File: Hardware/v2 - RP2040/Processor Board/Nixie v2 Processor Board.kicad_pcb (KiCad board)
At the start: 2 copper layers, 100 x 50 mm, 75 parts, among them J1 Conn_01x10_Socket, J2 Conn_01x10_Socket, J3 Conn_01x10_Socket, J4 Conn_01x01_Pin, J5 AudioJack3_SwitchT, J6 USB_C_Receptacle_USB2.0, J7 Conn_01x03_2.54mm, J8 Conn_01x03_2.54mm, SW1 SW_Push, SW2 SW_Push, SW3 SW_DIP_x10, SW4 SW_Push, U1 TPS82084SIL, U2 AP22913, U3 DS3231MZ, U4 RP2040, U5 W25Q128JVP, U6 MCP23017_ML, Y1 12MHz

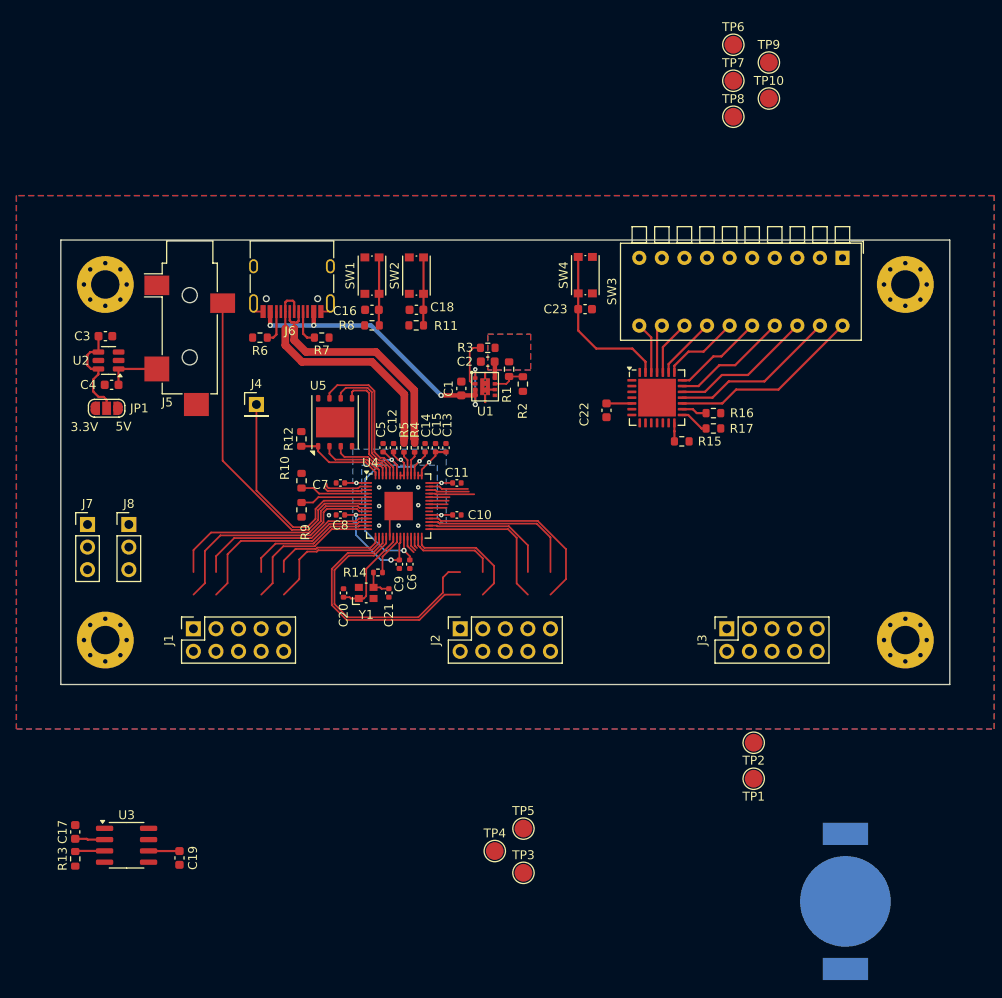
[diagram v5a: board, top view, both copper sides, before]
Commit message: finished initial layout and swapped SDA/SCL on connector
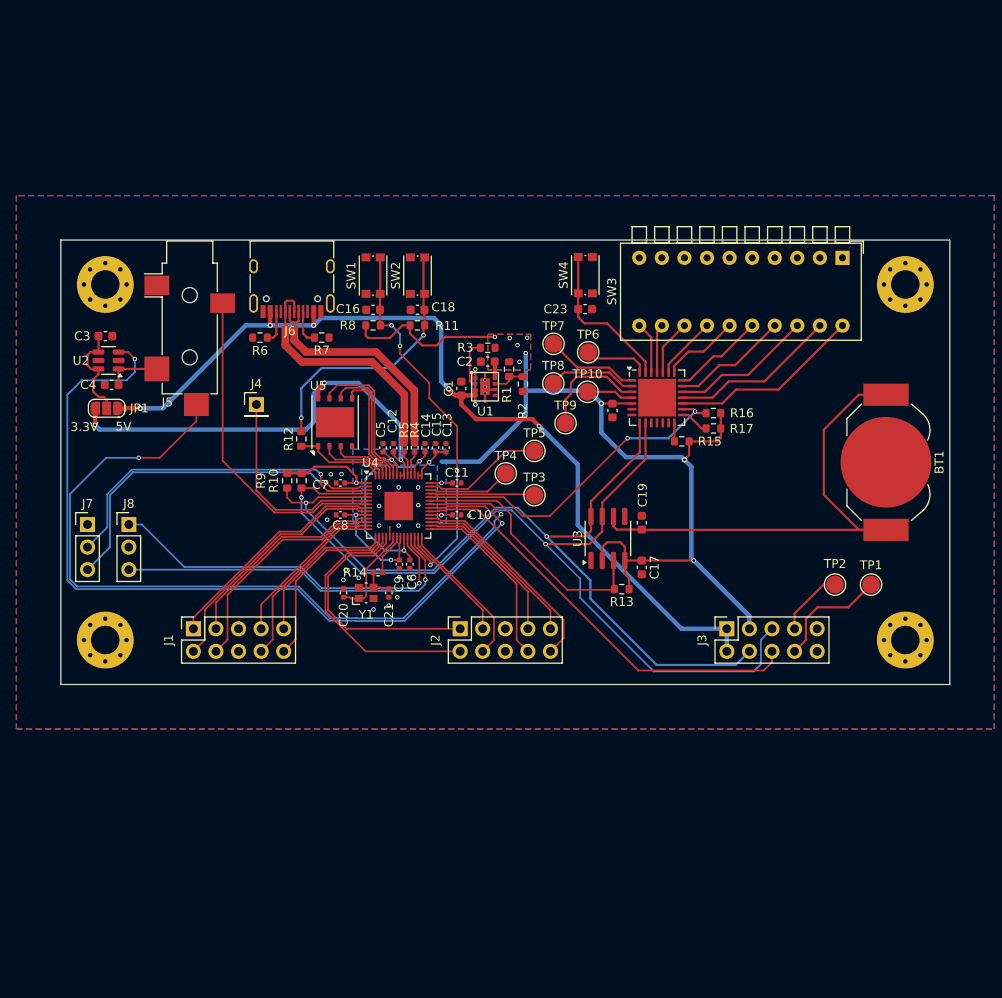
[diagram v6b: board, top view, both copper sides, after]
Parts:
- BT1: moved to F.Cu
- moved C17 70.3 mm to (165.3, 86.8), turned to -90 degrees
- moved R13 68.6 mm to (163.1, 89.3), turned to 180 degrees
- moved C19 64.2 mm to (165.3, 81.8), turned to 90 degrees
- moved U3 64.2 mm to (161.5, 83.6), turned to 90 degrees
- moved BT1 49.6 mm to (192.8, 75.0), turned to 90 degrees
- moved TP9 46.6 mm to (156.8, 70.6)
- moved TP3 42.5 mm to (153.3, 78.7)
- moved TP4 42.5 mm to (150.1, 76.2)
- moved TP5 42.5 mm to (153.3, 73.7)
- moved TP10 38.8 mm to (159.2, 67.1)
- moved TP6 38.3 mm to (159.3, 62.6)
- moved TP8 36.2 mm to (155.4, 66.1)
- moved TP7 35.8 mm to (155.4, 61.7)
- moved TP1 25.5 mm to (191.1, 88.8), turned to -90 degrees
- moved TP2 20.0 mm to (187.1, 88.8), turned to -90 degrees
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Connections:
- net /BOOT_SEL renamed Net-(U4-QSPI_SS)
- J3 pad 4: /I2C1_SDA -> /I2C1_SCL
- J3 pad 5: /I2C1_SCL -> /I2C1_SDA
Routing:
- net +3V3: track 38.1 -> 200.9 mm, vias 7 -> 18
- net /GPS_Enable: track 1.96 -> 97.6 mm, vias 0 -> 2
- net /I2C1_SDA: track 7.75 -> 102.8 mm, vias 0 -> 2
- net /GPS_Connected: track 2.09 -> 93.3 mm, vias 0 -> 2
- net /I2C1_SCL: track 7.74 -> 95.9 mm, vias 0 -> 2
- net VBUS: track 36.0 -> 109.3 mm, vias 5 -> 7
- net Net-(BT1-+): track 3.48 -> 56.6 mm
- net /Dimming: track 0.00 -> 47.8 mm
- net Net-(J8-Pin_1): track 2.05 -> 41.7 mm, vias 0 -> 1
- net Net-(J8-Pin_3): track 1.73 -> 40.7 mm, vias 0 -> 1
- net /UART0 TX: track 5.11 -> 40.3 mm, vias 0 -> 1
- net /RESET: track 9.07 -> 44.1 mm, vias 0 -> 4
- net /UART0 RX: track 5.06 -> 39.0 mm, vias 0 -> 1
- net /Settings_Interrupt: track 5.15 -> 38.5 mm, vias 0 -> 2
- net /RTC_Interrupt: track 5.51 -> 29.5 mm
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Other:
- board text removed: "DCDC"
- board text removed: "GPS"
- board text removed: "INTERCONNECT"
- board text removed: "RP2040"
- board text removed: "RTC"
- board text removed: "SETTINGS"
- board text removed: "USB"

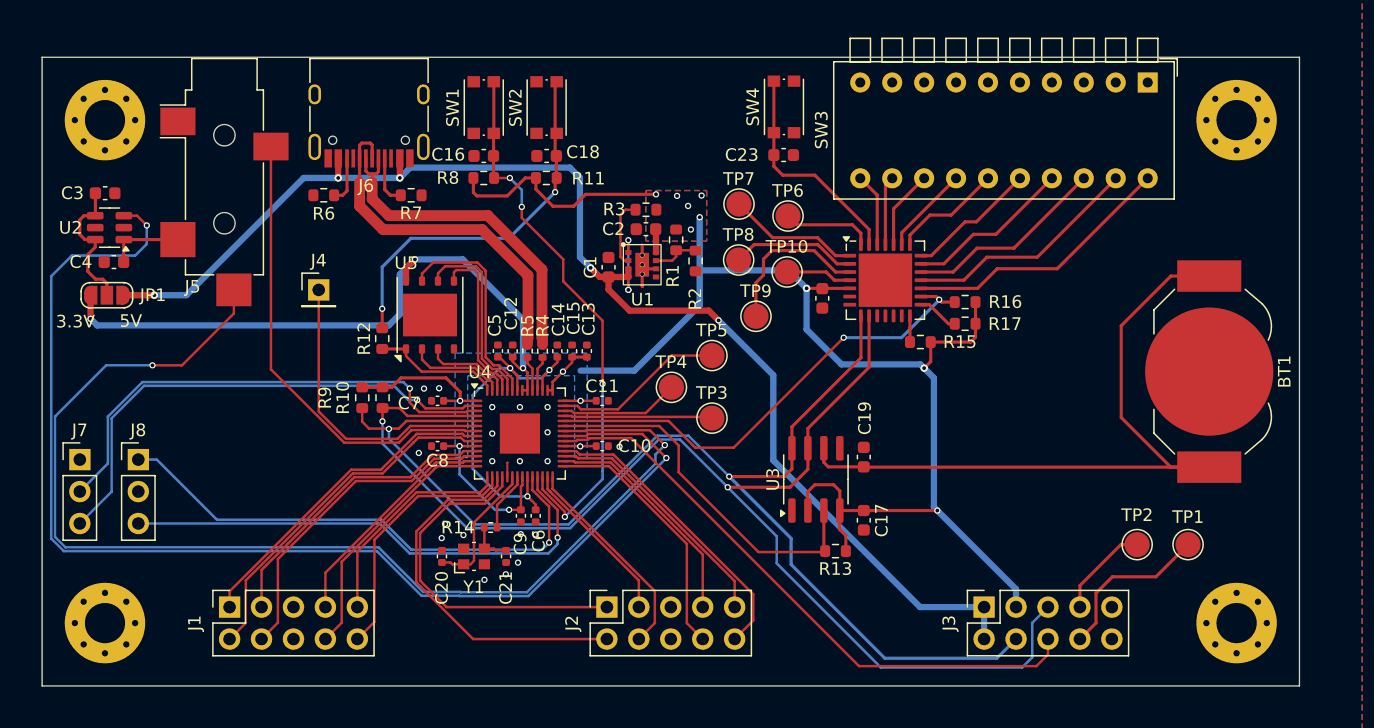
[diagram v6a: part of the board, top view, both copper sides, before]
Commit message: added ground via stitching, and baord names, version, designer, and date to silkscreen
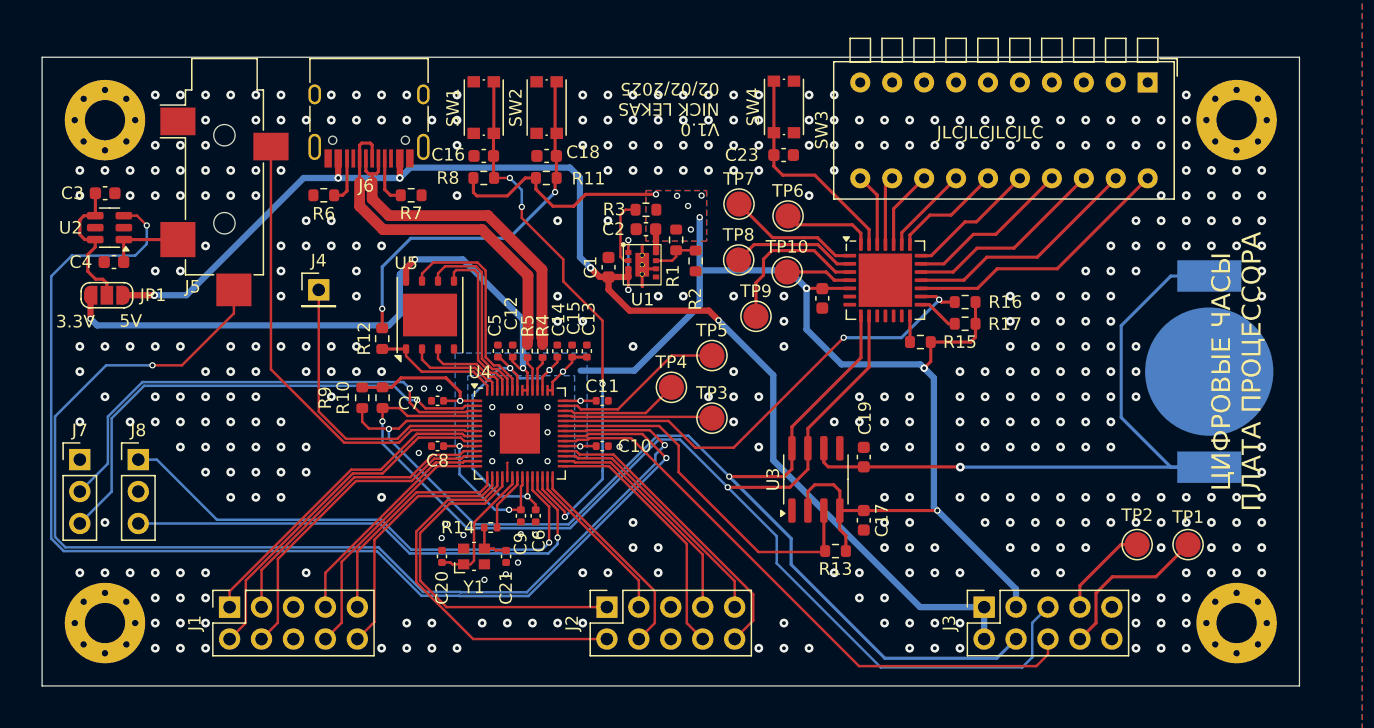
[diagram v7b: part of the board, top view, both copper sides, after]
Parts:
- BT1: moved to B.Cu
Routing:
- net Net-(BT1-+): vias 0 -> 1
- net GND: vias 20 -> 402
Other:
- board text added: "JLCJLCJLCJLC"
- board text added: "V1.0 NICK LEKAS 02/02/2025"
- board text added: "ЦИФРОВЫЕ ЧАСЫ ПЛАТА ПРОЦЕССОРА"
